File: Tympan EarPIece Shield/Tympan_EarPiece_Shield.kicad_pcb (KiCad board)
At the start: 4 copper layers, 38 x 40 mm, 47 parts, among them J1 Tympan_SJ-3523-SMT-TR, J2 Tympan_SJ-3524-SMT-TR-PI, J3 USB_B_Mini, J4 USB_B_Mini, P1 CONN_01X06, P2 CONN_01X06, P3 CONN_01X06, P4 CONN_01X06, P5 CONN_01X06, P6 CONN_01X06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

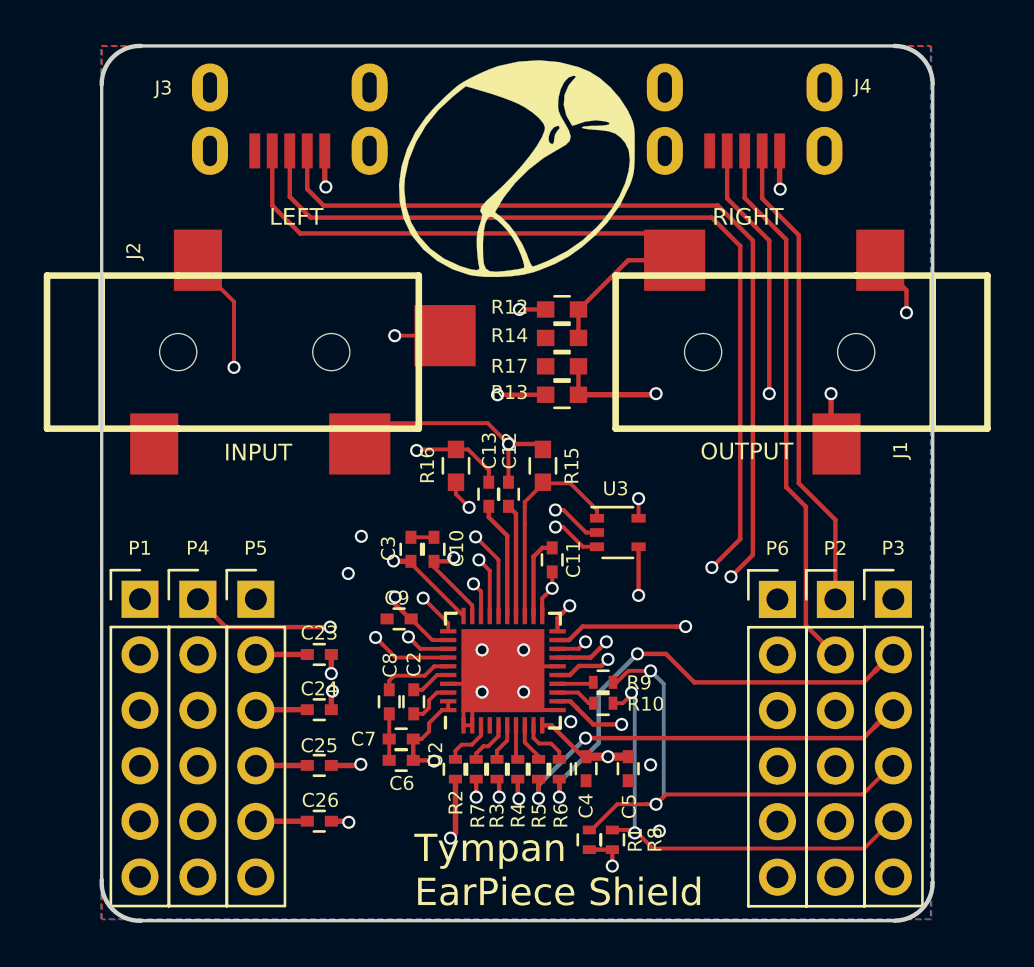
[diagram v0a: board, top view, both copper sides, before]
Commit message: Added mounting holes
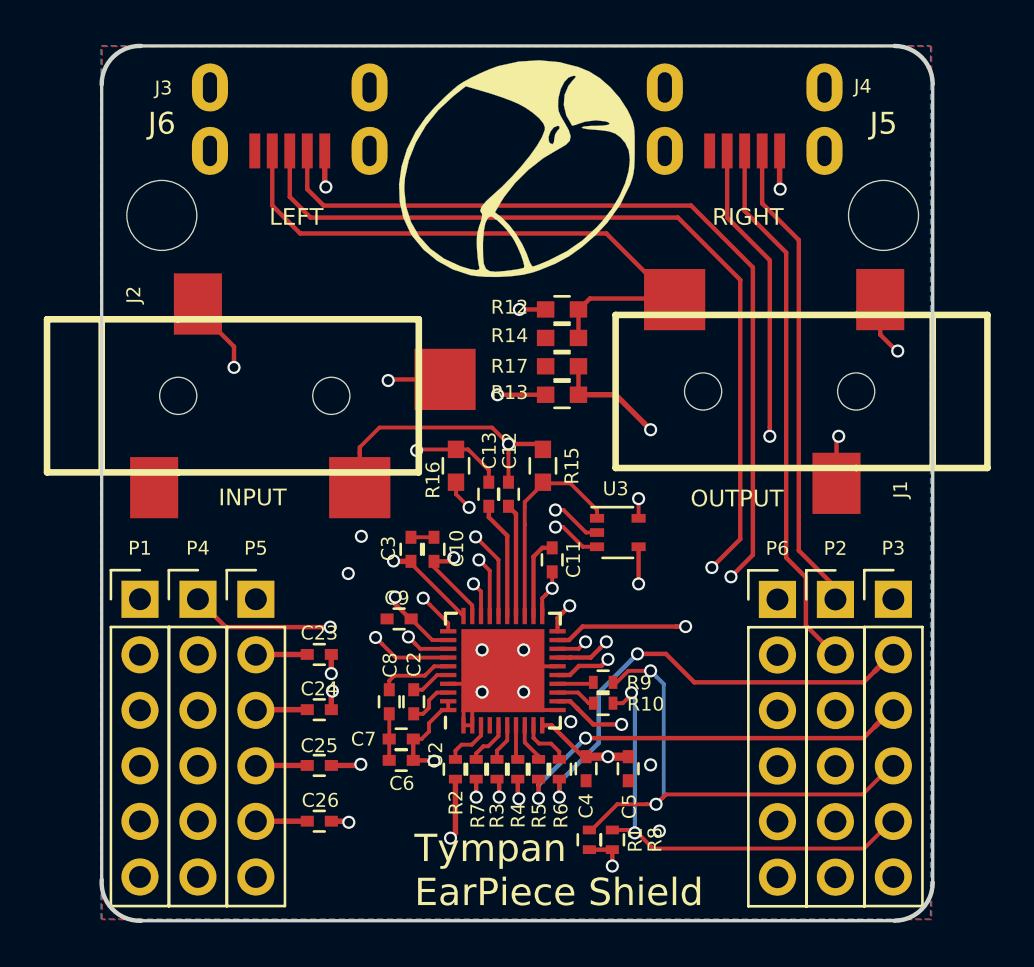
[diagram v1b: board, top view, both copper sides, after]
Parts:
- added J5: Conn_01x01, MountingHole:MountingHole_3.2mm_M3, F.Cu at (150.6, 54.2)
- added J6: Conn_01x01, MountingHole:MountingHole_3.2mm_M3, F.Cu at (117.6, 54.2)
- moved J2 2.00 mm to (118.3, 62.5)
- moved J1 1.80 mm to (149.3, 62.3)
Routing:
- net GND: track 79.9 -> 76.1 mm
- net /HPR_1: track 26.8 -> 30.0 mm
- net Net-(C12-Pad2): track 10.9 -> 12.7 mm
- net /MICDET: track 20.1 -> 18.4 mm
- net Net-(C13-Pad2): track 19.7 -> 18.0 mm
- net /PDM_CLK1: track 66.7 -> 65.8 mm
- net /PDM_DAT1: track 63.4 -> 62.7 mm
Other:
- outline, holes or cut-outs redrawn

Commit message: Adjusted top copper pour. Updated top image
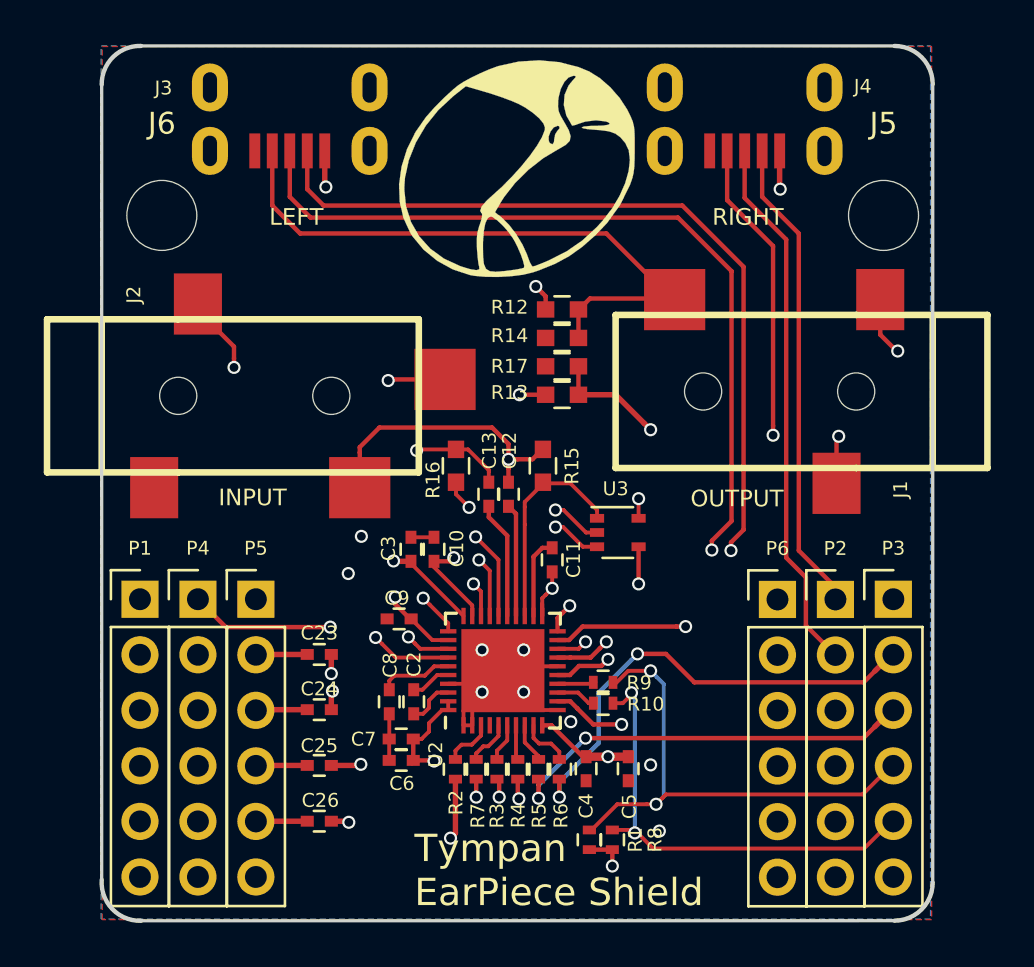
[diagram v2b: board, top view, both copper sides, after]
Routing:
- net Net-(R12-Pad1): track 18.2 -> 19.6 mm
- net /PDM_DAT1: track 62.7 -> 61.4 mm
- net /PDM_CLK1: track 65.8 -> 64.9 mm
- net Net-(R13-Pad1): track 17.0 -> 16.4 mm
